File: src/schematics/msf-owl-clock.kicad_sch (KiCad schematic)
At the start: 44 parts, among them U001 BC805M

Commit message: Started to draw the TFT module's schematic.
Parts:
- added C001, C002, C003, C004, C005, C006: 4.7μF, restall-generic-capacitors:unpolarised-nominal-0402-1005, symbol restall-generic-capacitors:capacitor-unpolarised
- added SHEET2: ~, symbol msf-owl-clock:2-msf-sensors-module
- renumbered C23 to C007, C22 to C008, C21 to C009, C001 to C010, C002 to C011, C003 to C012, D1 to D001
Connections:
- net BC805M_V_{DD}: now also FB001.1 (P1); no longer FB001.2 (P2)
- net GND: now also D004.2 (K), D004.4 (K), D004.5 (K), C001.2, C002.2, C003.2, C004.2, C005.2, C006.2
- net ~{BC805M_RESET}: now also CONN003.10 (~{RESET}), D001.4 (K), R006.1, R007.1, U001.4 (P021); no longer C007.1, R006.2, R21.2
- net CORE_VDD_{+3.3V}: now reaches CONN005.12 (TP_V_{DD})
- net CORE_VDD_{+3.3V}: now also CONN005.3 (V_{DDIO}), CONN005.6 (V_{DD}), CONN006.12 (TP_V_{DD}), CONN006.3 (V_{DDIO}), CONN006.6 (V_{DD}), FB001.2 (P2), R20.2, C001.1, C002.1, C003.1, C004.1, C005.1, C006.1
- removed net 1-usb-and-power/CORE_VDD_{+3.3V}: FB001.1 (P1), R20.2
- new net: C007.1, R006.2, R21.2
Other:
- sheet 6-tft-driver ports: added CORE_VDD_{+3.3V}, CORE_VDD_{+5V}; removed none
- note added: "CONNECTOR - OK-14F024-04"
- note added: "TODO: CHECK DATASHEETS AFTER COMPLETED THE LAYOUT - REMOVE ANY FOR PARTS THAT ARE NOT USED (PERHAPS MMBT3904 ?) AND ADD ANY THAT ARE MISSING."
- note added: "TODO: THESE PIN NUMBERS NEED SORTING - DOESN'T SEEM LIKE THEY ARE CORRECT FOR THE MATING ORIENTATION..."
- note removed: "POWER DOMAINS: USB VBUS -> BUCK 3.3V, 2A (~2.25MHz) - TPS628512 (is L current acceptable for USB specs ?) -> USB SUPPORT (FUSB302, ETC.) MCU BC805M TFT LDO 2.8V -> SENSORS LOAD SWITCH -> SD Card LOAD SWITCH -> Audio LDO 3.6V -> MSF RECEIVER"
- moved on the sheet: C007, C008, C009, CONN005, CONN006, FB001, R21

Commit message: Drew the schematic for the TFT driver.
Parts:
- added SHEET3: ~, symbol msf-owl-clock:6-msf-tft-driver-module
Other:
- sheet 3-mcu-core ports: added TFT_I^{2}C_SEL, TFT_QSPI_SEL; removed TFT_SEL
- sheet 6-tft-driver ports: added TFT_I^{2}C_SEL, TFT_QSPI_SEL; removed TFT_SEL
- note added: "TODO: DOUBLE-CHECK THESE PIN NUMBERS - THEY LOOK CORRECT BUT TRY AN ACTUAL CONNECTION (1 -> 12, 24 -> 13"
- note removed: "TODO: THESE PIN NUMBERS NEED SORTING - DOESN'T SEEM LIKE THEY ARE CORRECT FOR THE MATING ORIENTATION..."
- moved on the sheet: SPK001

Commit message: Added the infrared receiver.  Various tidy-ups.
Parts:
- added C009: 4.7μF, restall-generic-capacitors:unpolarised-nominal-0402-1005, symbol restall-generic-capacitors:capacitor-unpolarised
- added SHEET003: ~, symbol msf-owl-clock:3-msf-mcu-core-module
- added U002: TSOP75338TT, restall-manufacturer-vishay:TSOP7????TT, symbol restall-manufacturer-vishay:TSOP75???T?
- renumbered C009 to C001, C008 to C002, C001 to C003, C002 to C004, C003 to C005, C004 to C006, C005 to C007, C006 to C008, SHEET101 to SHEET001, SHEET102 to SHEET002, SHEET1 to SHEET004, SHEET2 to SHEET005, SHEET3 to SHEET006
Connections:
- net CORE_VDD_{+3.3V}: now also C009.1, U002.1 (V_{SS}), U002.4 (V_{SS})
- net GND: now also C009.2, U002.2 (V_{DD})
- new net 3-mcu-core/IR_RCV_DATA: U002.3 (OUT)
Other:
- sheet 3-mcu-core ports: added IR_RCV_DATA; removed {IR_RCV}
- note added: "TODO: FOOTPRINT FOR SD CARD !"
- note added: "TODO: FOOTPRINTS FOR ARM CONNECTORS"

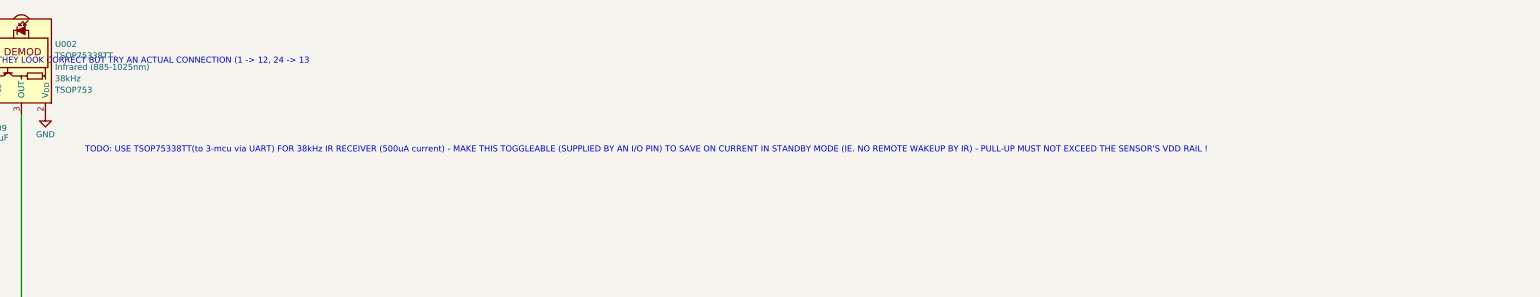
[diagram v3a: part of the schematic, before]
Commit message: Started to determine the series terminations for the various high-speed links.
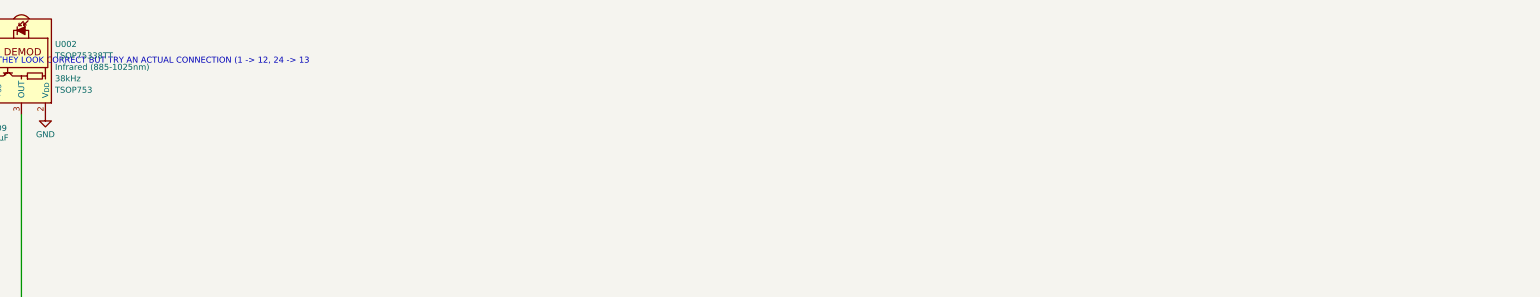
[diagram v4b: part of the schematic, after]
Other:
- note removed: "TODO: USE TSOP75338TT(to 3-mcu via UART) FOR 38kHz IR RECEIVER (500uA current) - MAKE THIS TOGGLEABLE (SUPPLIED BY AN I/O PIN) TO SAVE ON CURRENT IN STANDBY MODE (IE. NO REMOTE WAKEUP BY IR) - PULL-UP MUST NOT EXCEED THE SENSOR'S VDD RAIL !"
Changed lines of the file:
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@@
-    (effects (font (size 1.27 1.27)) (justify left bottom))
-  )
-  (text "TODO: USE TSOP75338TT(to 3-mcu via UART) FOR 38kHz IR RECEIVER (500uA current) - MAKE THIS TOGGLEABLE (SUPPLIED BY AN I/O PIN) TO SAVE ON CURRENT IN STANDBY MODE (IE. NO REMOTE WAKEUP BY IR) - PULL-UP MUST NOT EXCEED THE SENSOR'S VDD RAIL !\n"
-    (at 386.842 55.118 0)
     (effects (font (size 1.27 1.27)) (justify left bottom))
   )

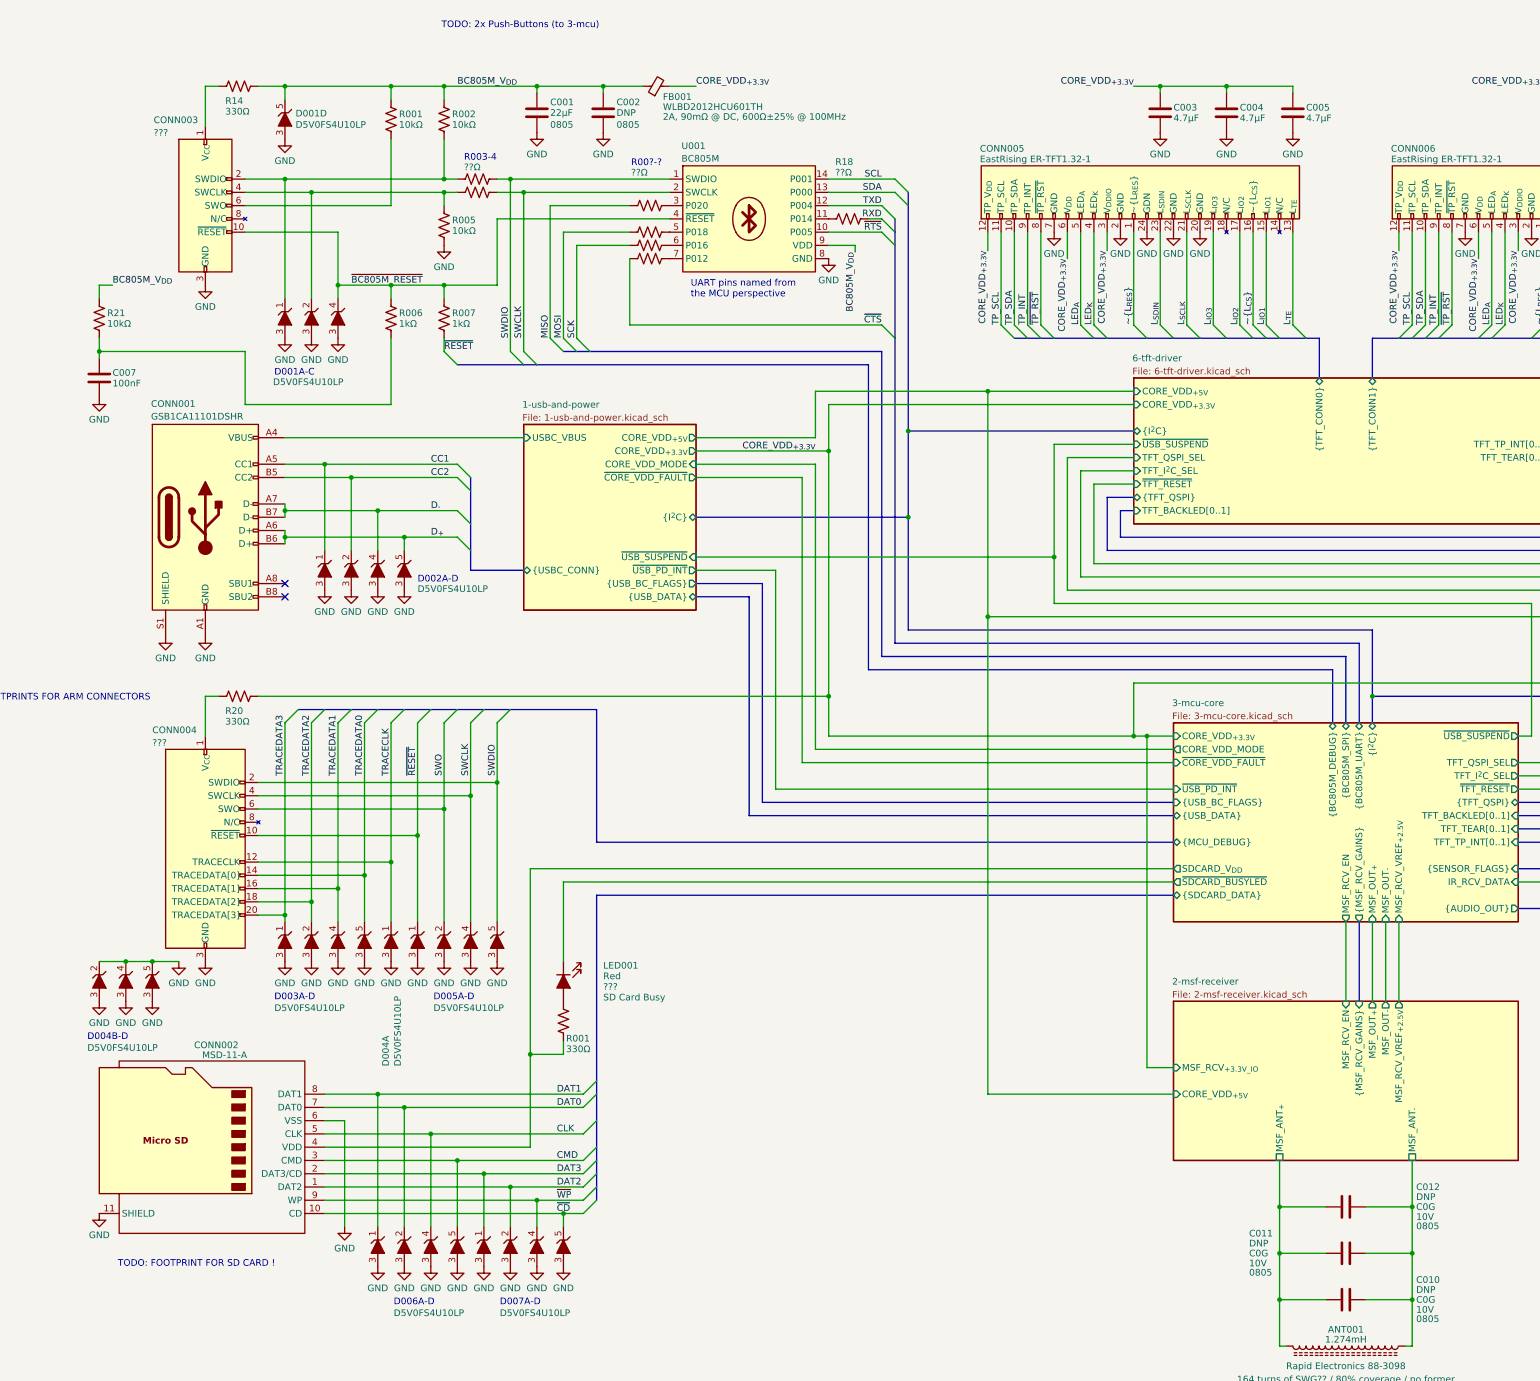
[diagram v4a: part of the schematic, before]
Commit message: Further elaboration of the circuitry surrounding the microcontroller.
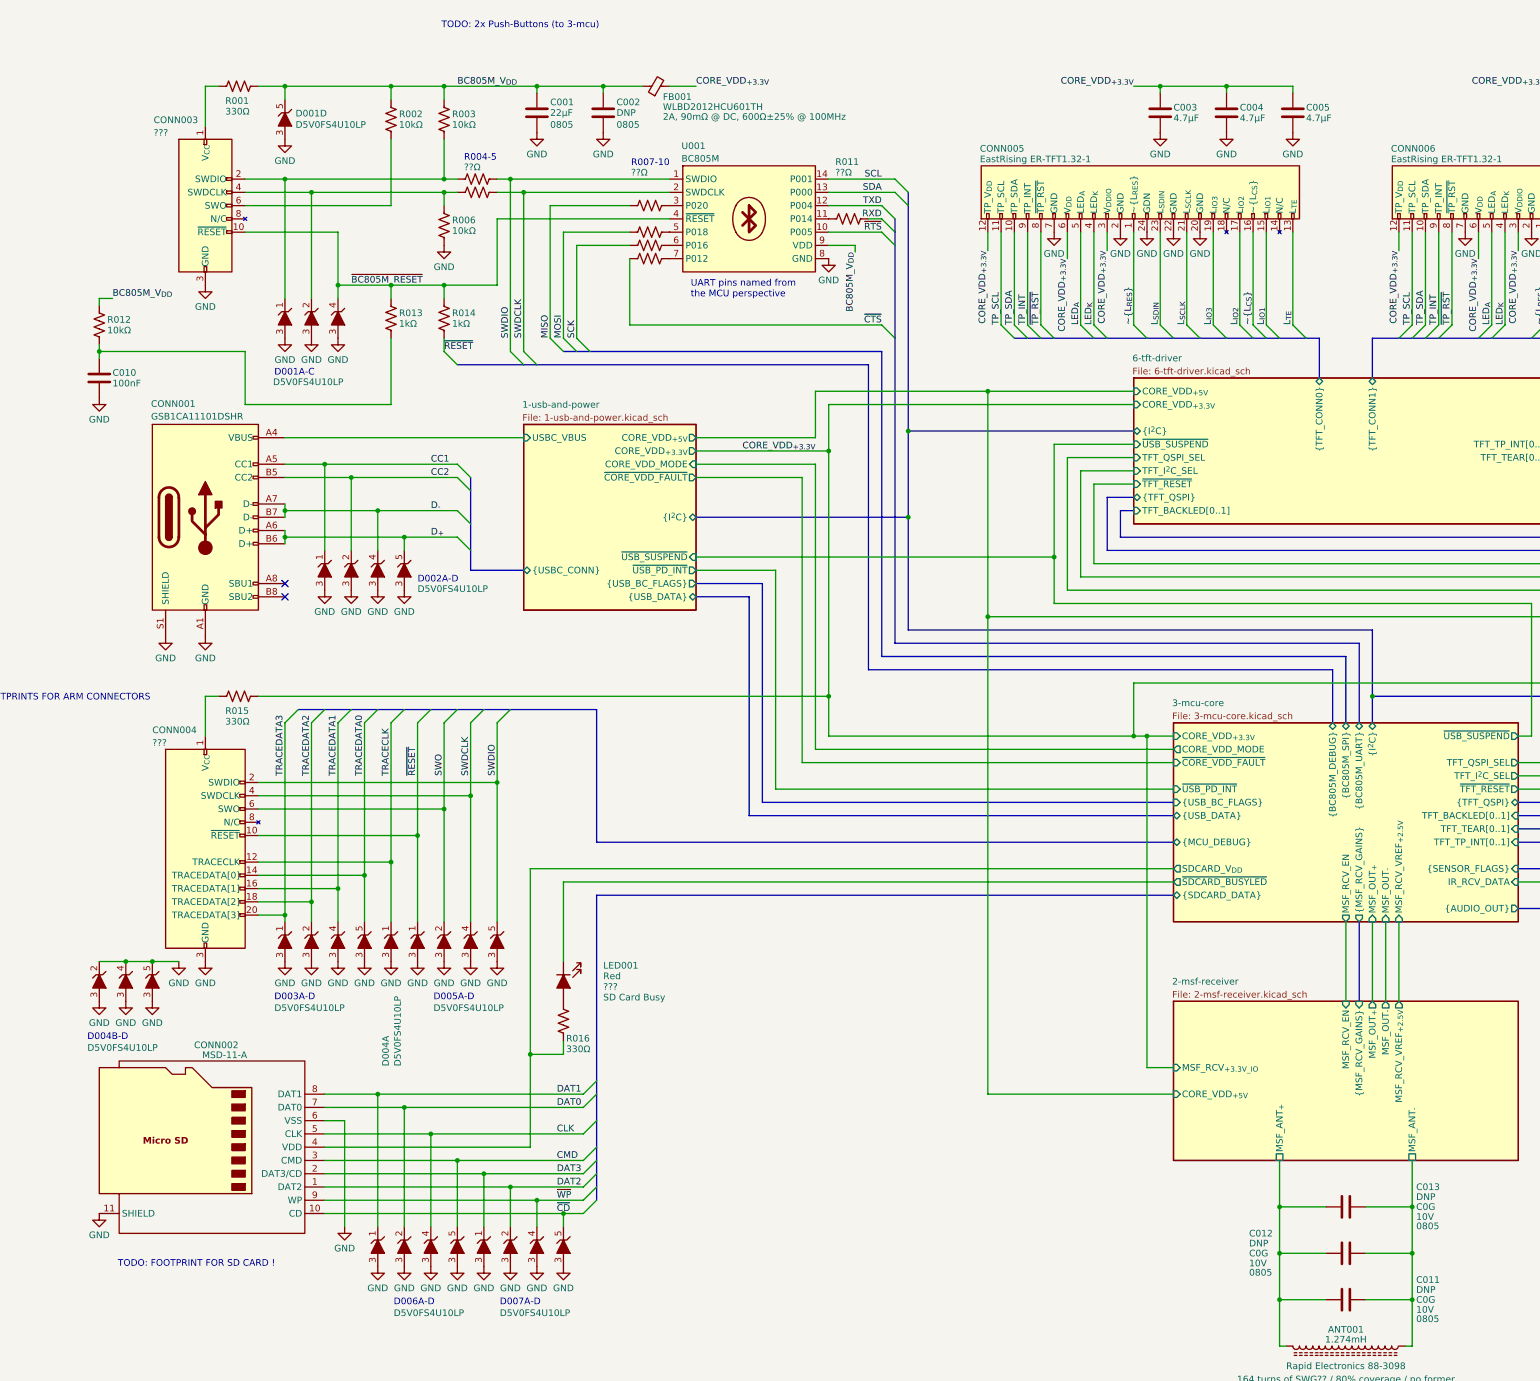
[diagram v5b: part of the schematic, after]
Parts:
- renumbered C007 to C010, C010 to C011, C011 to C012, C012 to C013, R14 to R001, R001 to R002, R002 to R003, R003 to R004, R004 to R005, R005 to R006, R15 to R007, R16 to R008, R17 to R009, R19 to R010, R18 to R011, R21 to R012, R006 to R013, R007 to R014, R20 to R015, R001 to R016
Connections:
- net SWCLK renamed SWDCLK
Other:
- note added: "R004-5"
- note added: "R007-10"
- note removed: "R003-4"
- note removed: "R00?-?"
- moved on the sheet: R012

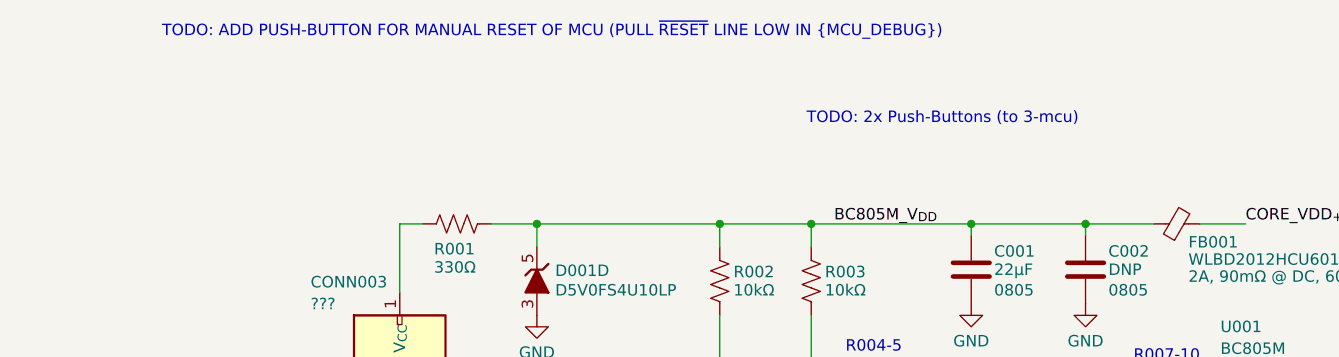
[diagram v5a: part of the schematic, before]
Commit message: Further elaboration of the circuitry surrounding the microcontroller.
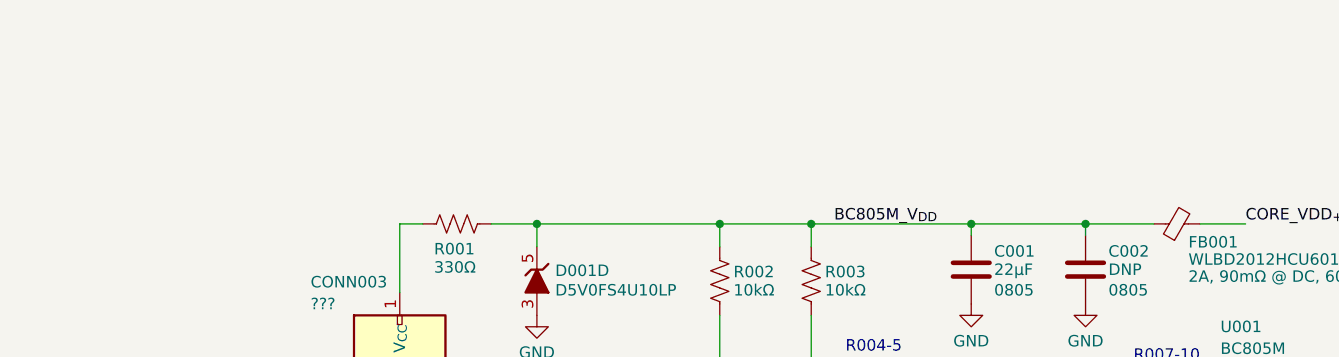
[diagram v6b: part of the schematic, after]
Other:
- note removed: "TODO: 2x Push-Buttons (to 3-mcu)"
- note removed: "TODO: ADD PUSH-BUTTON FOR MANUAL RESET OF MCU (PULL ~{RESET} LINE LOW IN {MCU_DEBUG})"
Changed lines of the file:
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@@
-    (effects (font (size 1.27 1.27)) (justify left bottom))
-  )
-  (text "TODO: 2x Push-Buttons (to 3-mcu)" (at 83.312 4.318 0)
     (effects (font (size 1.27 1.27)) (justify left bottom))
   )
@@
     (effects (font (size 1.27 1.27)) (justify left bottom))
   )
-  (text "TODO: ADD PUSH-BUTTON FOR MANUAL RESET OF MCU (PULL ~{RESET} LINE LOW IN {MCU_DEBUG})"
-    (at 11.684 -5.334 0)
-    (effects (font (size 1.27 1.27)) (justify left bottom))
-  )

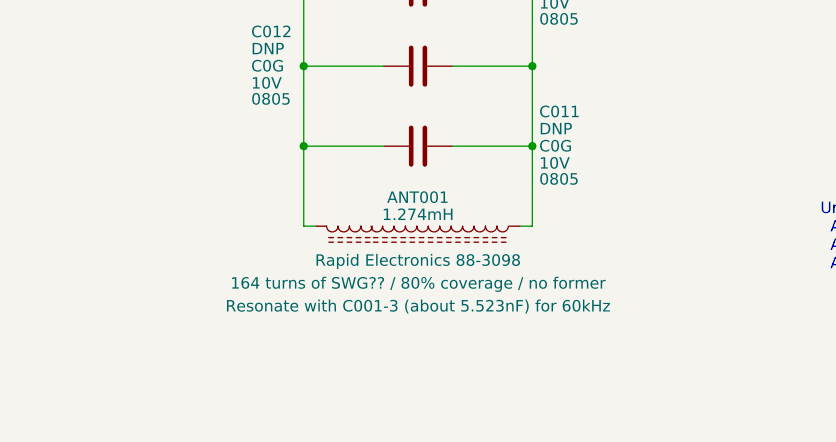
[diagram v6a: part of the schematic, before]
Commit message: Further elaboration of the circuitry surrounding the microcontroller.  Plus a few typos / tidy-ups.
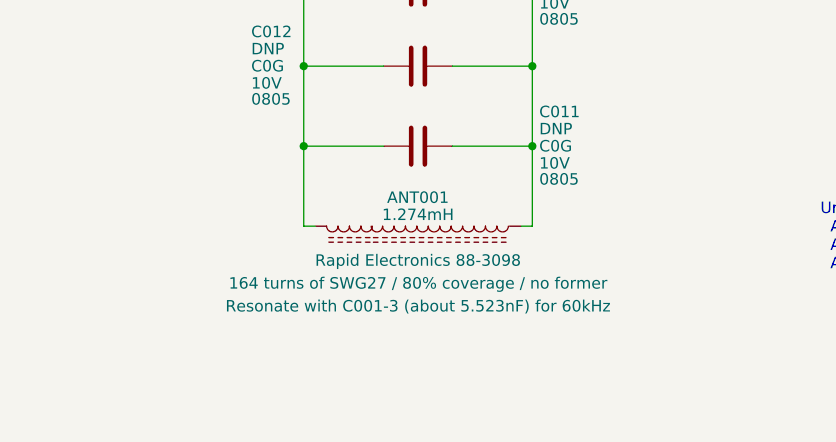
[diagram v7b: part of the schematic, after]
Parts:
- ANT001: Windings 164 turns of SWG?? / 80% coverage / no former -> 164 turns of SWG27 / 80% coverage / no former
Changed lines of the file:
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@@
       (effects (font (size 1.27 1.27)) (justify left) hide)
     )
-    (property "Windings" "164 turns of SWG?? / 80% coverage / no former" (at 256.54 262.89 0)
+    (property "Windings" "164 turns of SWG27 / 80% coverage / no former" (at 256.54 262.89 0)
       (effects (font (size 1.27 1.27)))
     )

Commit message: Various tidy-ups and checks, mainly around the bypass capacitors.  Added a load of test points.
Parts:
- added C001: 4.7μF, restall-generic-capacitors:unpolarised-nominal-0402-1005, symbol restall-generic-capacitors:capacitor-unpolarised
- renumbered C001 to C002, C002 to C003, C003 to C004, C004 to C005, C005 to C006, C006 to C007, C007 to C008, C008 to C009, C009 to C010, C010 to C011, C011 to C012, C012 to C013, C013 to C014
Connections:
- net BC805M_V_{DD}: now also C001.1
- net GND: now also C001.2
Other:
- note removed: "TODO: 60x 4.7uF 0402 bypass caps plus 22uF bulk next to BC805M = about maximum C for the +3.3V line."
- moved on the sheet: C002, C003, FB001
